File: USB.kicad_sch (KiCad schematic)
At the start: 7 parts, among them J1 USB_C_Receptacle, U1 CM5104032, U2 TPD6E05U06RVZ, U3 TPD6E05U06RVZ, U4 HD3SS3220

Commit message: added git ignore
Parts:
- added C3: 100n, symbol Device:C_Small
- added U5: TPD4S201, symbol DIY Pi Smartphone Library:TPD4S201
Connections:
- net GND: now also C3.1, U5.1 (C_SBU1), U5.13 (GND), U5.14 (SBU2), U5.15 (SBU1), U5.18 (GND), U5.2 (C_SBU2), U5.8 (GND), U5.TP
- net USB_CC1: now also U5.4 (C_CC1), U5.7 (RPD_G1); no longer U4.2 (CC1)
- net USB_CC2: now also U5.5 (C_CC2), U5.6 (RPD_G2); no longer U4.1 (CC2)
- net VBUS: now reaches J1.A4 (VBUS), J1.A9 (VBUS), J1.B4 (VBUS), J1.B9 (VBUS)
- new net: C3.2, U5.3 (VBIAS)
- new net CC1: U4.2 (CC1), U5.12 (CC1)
- new net CC2: U4.1 (CC2), U5.11 (CC2)
- no-connect marks 0 -> 2
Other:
- moved on the sheet: U3, U4

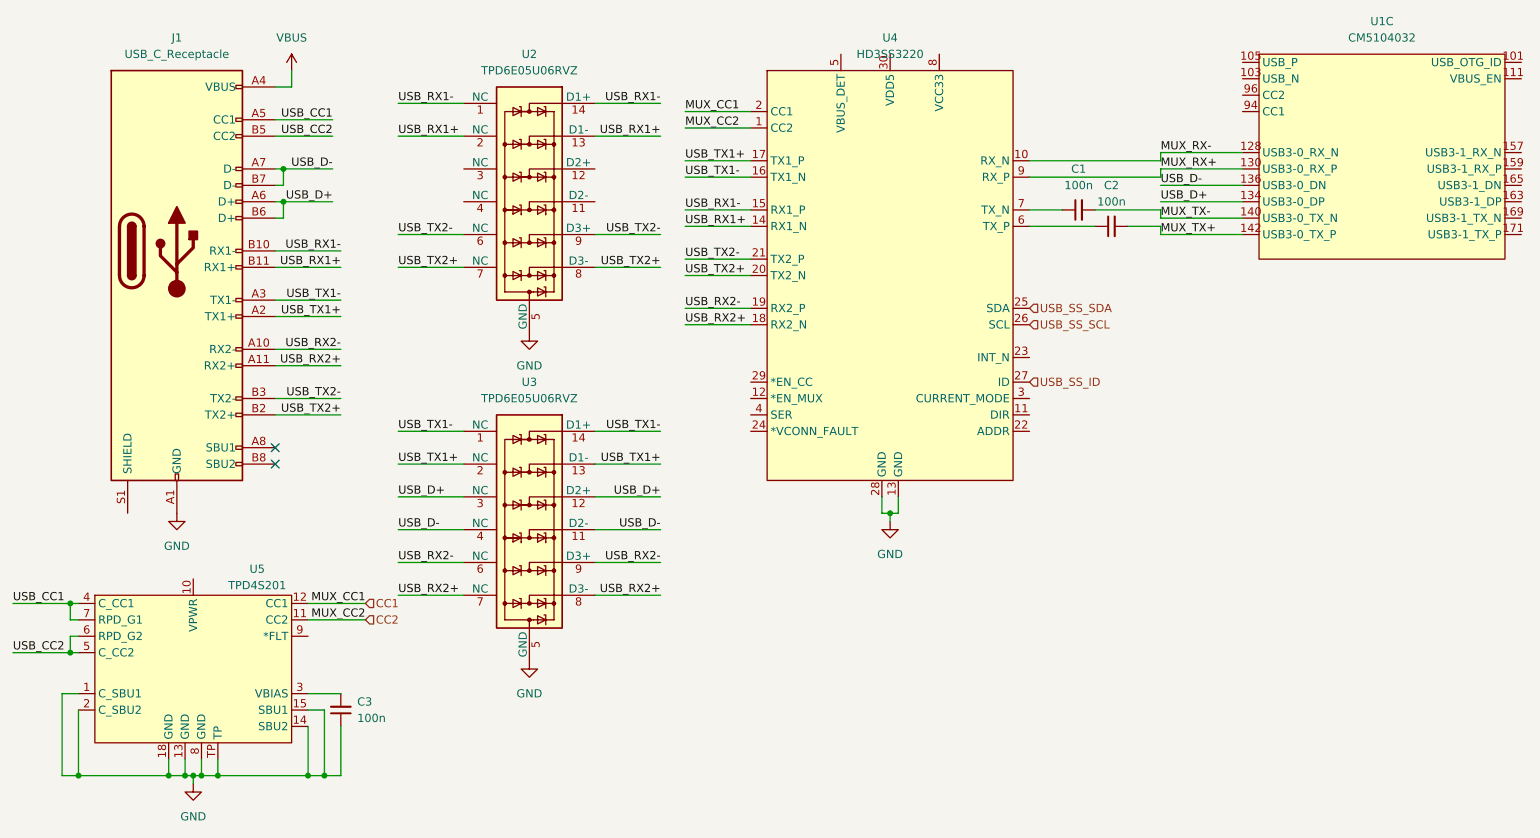
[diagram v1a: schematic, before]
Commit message: added PD TPS65987D and CHG BQ25895
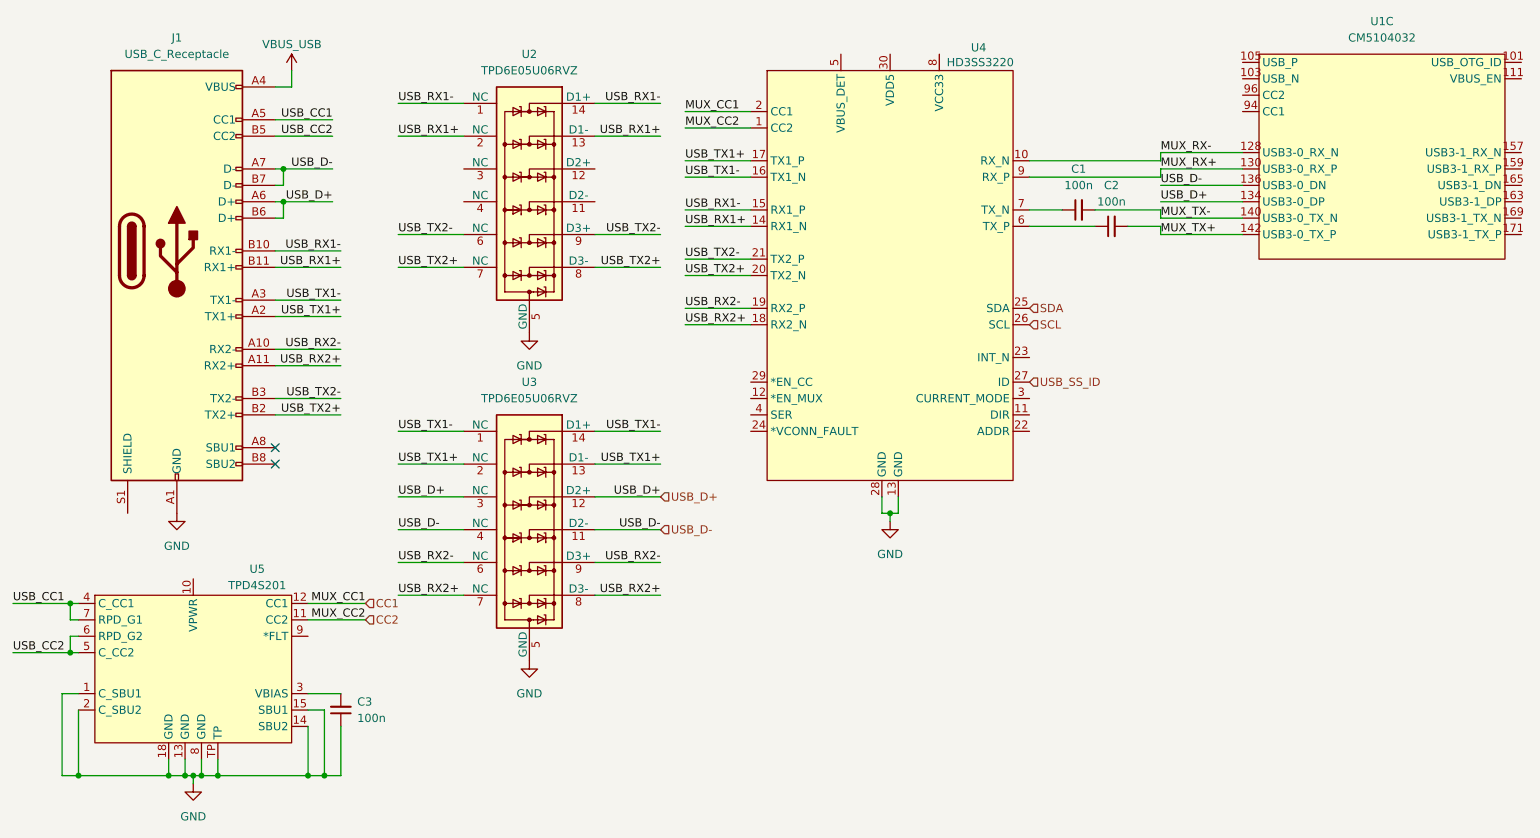
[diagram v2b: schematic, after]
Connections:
- net USB_SS_SCL renamed SCL
- net USB_SS_SDA renamed SDA
- net VBUS renamed VBUS_USB
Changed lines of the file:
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@@
 		)
 	)
-	(hierarchical_label "USB_SS_SCL"
+	(hierarchical_label "SCL"
 		(shape input)
 		(at 195.58 110.49 0)
@@
 		)
 	)
+	(hierarchical_label "USB_D-"
+		(shape input)
+		(at 138.43 142.24 0)
+		(effects
+			(font
+				(size 1.27 1.27)
+			)
+			(justify left)
+		)
+	)
+	(hierarchical_label "USB_D+"
+		(shape input)
+		(at 138.43 137.16 0)
+		(effects
+			(font
+				(size 1.27 1.27)
+			)
+			(justify left)
+		)
+	)
 	(hierarchical_label "CC1"
 		(shape input)
@@
 		)
 	)
-	(hierarchical_label "USB_SS_SDA"
+	(hierarchical_label "SDA"
 		(shape input)
 		(at 195.58 107.95 0)
@@
 		(on_board yes)
 		(dnp no)
-		(fields_autoplaced yes)
 		(property "Reference" "#PWR06"
 			(at 81.28 74.93 0)
@@
 			)
 		)
-		(property "Value" "VBUS"
-			(at 81.28 66.04 0)
-			(effects
-				(font
-					(size 1.27 1.27)
-				)
+		(property "Value" "VBUS_USB"
+			(at 76.708 67.056 0)
+			(effects
+				(font
+					(size 1.27 1.27)
+				)
+				(justify left)
 			)
 		)
@@
 		(on_board yes)
 		(dnp no)
-		(fields_autoplaced yes)
 		(property "Reference" "U4"
-			(at 173.99 66.04 0)
+			(at 187.706 67.564 0)
 			(effects
 				(font
@@
 		)
 		(property "Value" "HD3SS3220"
-			(at 173.99 68.58 0)
-			(effects
-				(font
+			(at 187.96 69.85 0)
+			(effects
+				(font

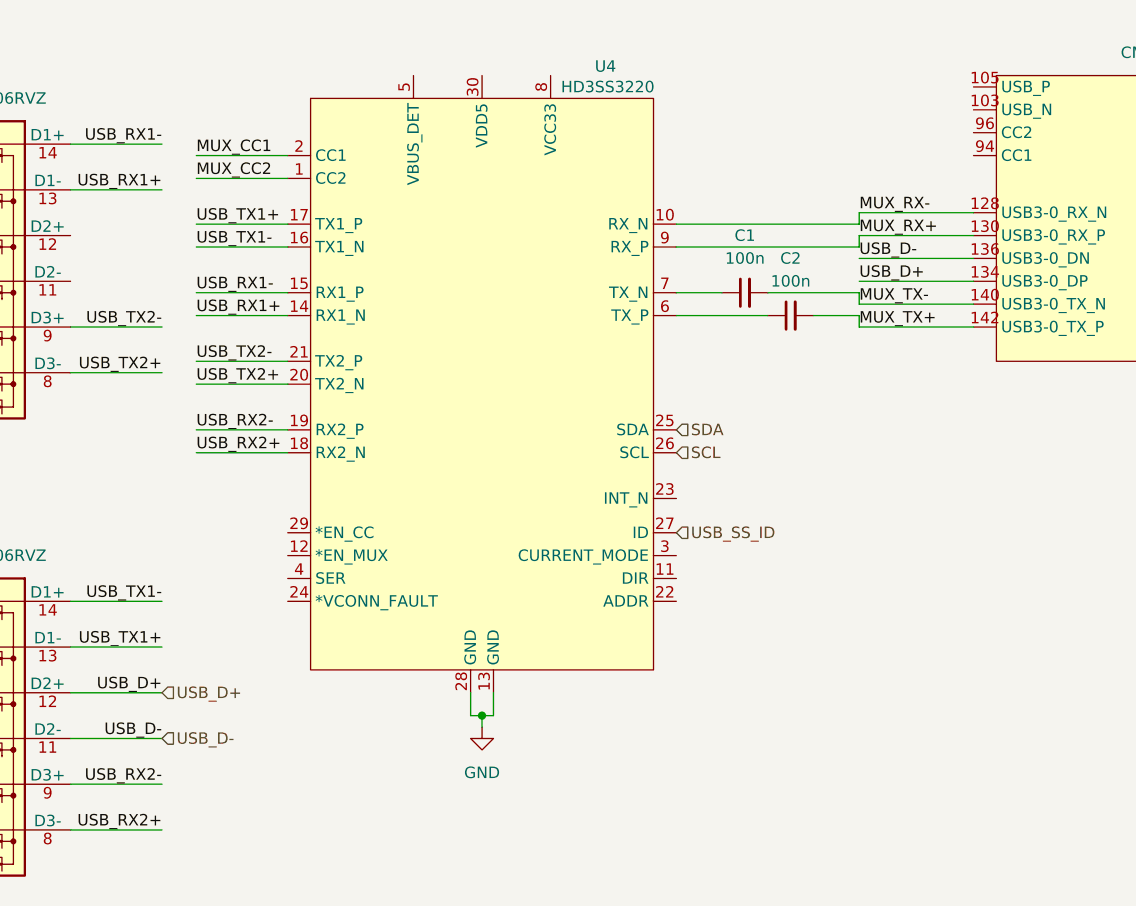
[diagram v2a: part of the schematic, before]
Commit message: added MAX177330 CHG
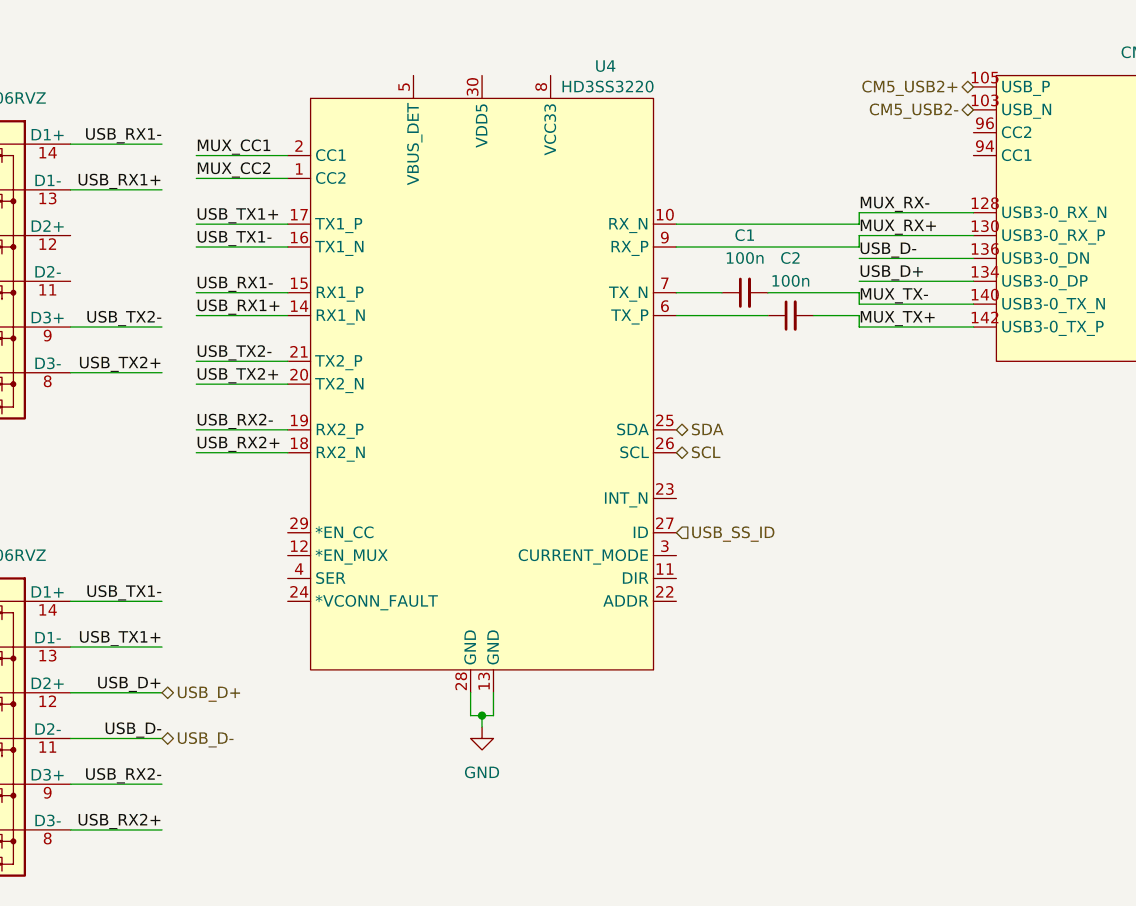
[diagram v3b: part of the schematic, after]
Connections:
- net CM5_USB2-: now reaches U1.103 (USB_N)
- net CM5_USB2+: now reaches U1.105 (USB_P)
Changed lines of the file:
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@@
 	)
 	(hierarchical_label "SCL"
-		(shape input)
+		(shape bidirectional)
 		(at 195.58 110.49 0)
 		(effects
@@
 			)
 			(justify left)
+		)
+	)
+	(hierarchical_label "CM5_USB2-"
+		(shape bidirectional)
+		(at 228.6 72.39 180)
+		(effects
+			(font
+				(size 1.27 1.27)
+			)
+			(justify right)
 		)
 	)
@@
 	)
 	(hierarchical_label "USB_D-"
-		(shape input)
+		(shape bidirectional)
 		(at 138.43 142.24 0)
 		(effects
@@
 		)
 	)
+	(hierarchical_label "CM5_USB2+"
+		(shape bidirectional)
+		(at 228.6 69.85 180)
+		(effects
+			(font
+				(size 1.27 1.27)
+			)
+			(justify right)
+		)
+	)
 	(hierarchical_label "USB_D+"
-		(shape input)
+		(shape bidirectional)
 		(at 138.43 137.16 0)
 		(effects
@@
 	)
 	(hierarchical_label "SDA"
-		(shape input)
+		(shape bidirectional)
 		(at 195.58 107.95 0)
 		(effects
